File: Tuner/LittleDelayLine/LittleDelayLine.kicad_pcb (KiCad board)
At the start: 2 copper layers, 100 x 100 mm, 114 parts, among them J1 Conn_Coaxial, J10 Conn_Coaxial, J11 Conn_02x05_Odd_Even, J12 Conn_01x01, J13 Conn_01x01, J14 Conn_01x01, J15 Conn_01x01, J16 Conn_01x01, J17 Conn_Coaxial, J18 Conn_01x01, J19 Conn_01x01, J2 Conn_Coaxial, J20 Conn_01x01, J21 Conn_01x01, J22 Conn_Coaxial, J23 Conn_Coaxial, J24 Conn_Coaxial, J25 Conn_01x01, J26 Conn_01x01, J27 Conn_01x01, J3 Conn_Coaxial, J4 Conn_Coaxial, J5 Conn_Coaxial, J6 Conn_Coaxial, J7 Conn_Coaxial, J8 Conn_01x02, J9 Conn_01x02, P10 Conn_01x01, P11 Conn_01x01, P12 Conn_01x01, P2 Conn_01x01, P3 Conn_01x01, P4 Conn_01x01, P5 Conn_01x01, P6 Conn_01x01, P7 Conn_01x01, P8 Conn_01x01, P9 Conn_01x01, U1 MCP23008, U2 ULN2803A

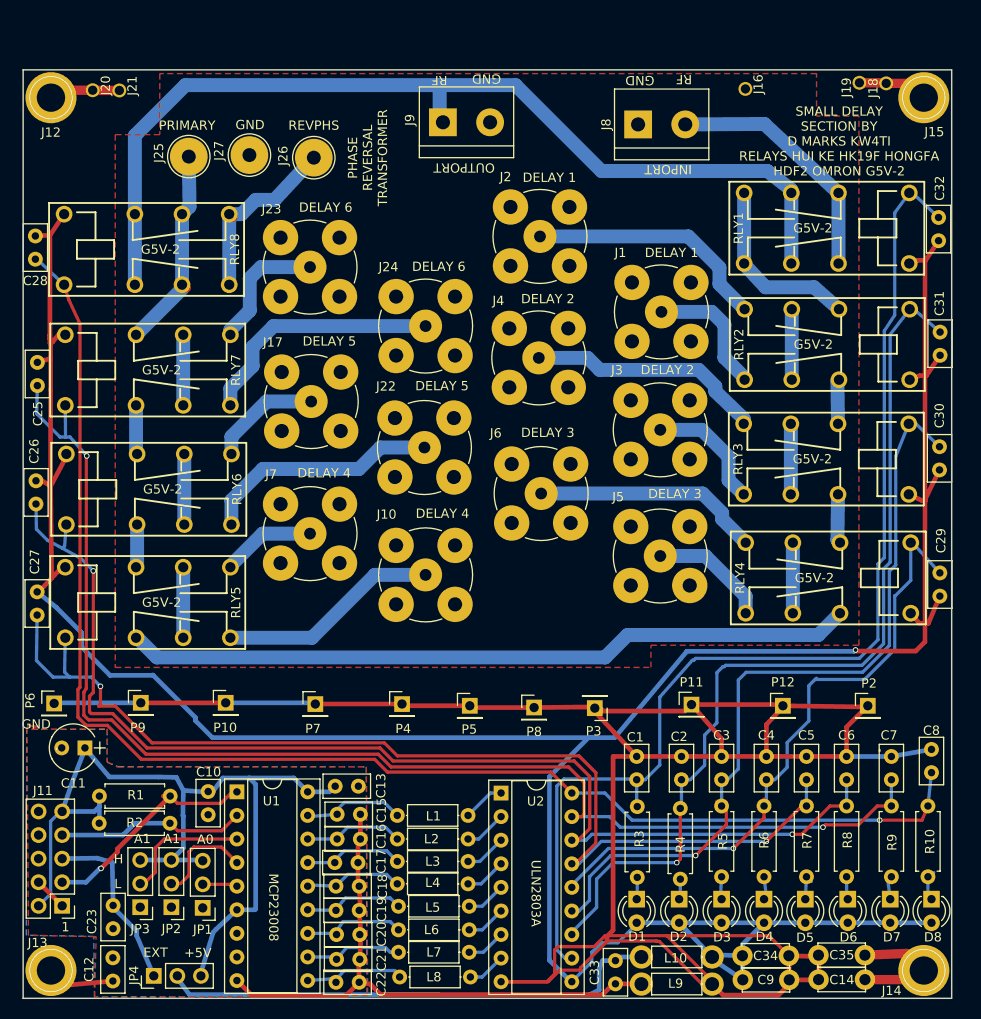
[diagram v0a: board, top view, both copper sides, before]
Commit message: Added more instrumentation to TandemMatch, fixed grounding issue
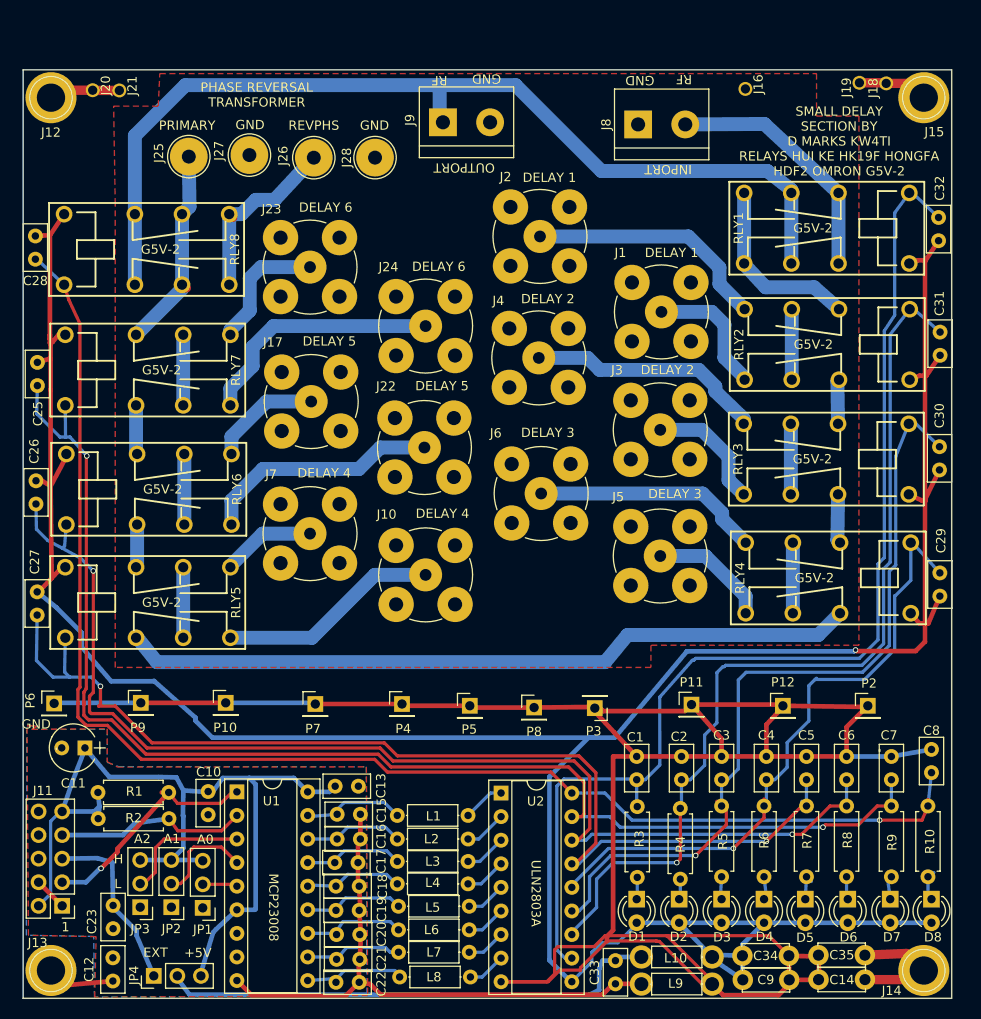
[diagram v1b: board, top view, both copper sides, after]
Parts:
- added J28: Conn_01x01, Connectors:1pin, F.Cu at (87.9, 59.5)
- R1, R2: value 1k -> 10k
- moved R2 0.50 mm to (58.1, 130.6)
- moved R1 0.42 mm to (58.1, 127.8)
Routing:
- net Net-(RLY4-Pad2): track 78.7 -> 79.4 mm
- net SCL: track 24.5 -> 25.0 mm
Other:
- board text added: "A2"
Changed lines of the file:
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@@
 (kicad_pcb (version 4) (host pcbnew 4.0.7)
   (general
-    (links 255)
+    (links 256)
     (no_connects 0)
-    (area 49.924999 49.924999 150.075001 150.075001)
+    (area 44.281218 46.80968 152.3901 153.921938)
     (thickness 1.6)
-    (drawings 40)
+    (drawings 41)
     (tracks 728)
     (zones 0)
-    (modules 114)
+    (modules 115)
     (nets 77)
   )
@@
   )
   (setup
-    (last_trace_width 0.5)
+    (last_trace_width 0.25)
     (user_trace_width 0.35)
     (user_trace_width 0.5)
@@
   )
   (module Resistors_THT:R_Axial_DIN0207_L6.3mm_D2.5mm_P7.62mm_Horizontal (layer F.Cu)
-    (at 58.2168 128.2192)
+    (at 58.05932 127.8255)
     (descr "Resistor, Axial_DIN0207 series, Axial, Horizontal, pin pitch=7.62mm, 0.25W = 1/4W, length*diameter=6.3*2.5mm^2, http://cdn-reichelt.de/documents/datenblatt/B400/1_4W%23YAG.pdf")
     (tags "Resistor Axial_DIN0207 series Axial Horizontal pin pitch 7.62mm 0.25W = 1/4W length 6.3mm diameter 2.5mm")
@@
       (effects (font (size 1 1) (thickness 0.15)))
     )
-    (fp_text value 1k (at 3.81 2.31) (layer F.Fab)
+    (fp_text value 10k (at 3.81 2.31) (layer F.Fab)
       (effects (font (size 1 1) (thickness 0.15)))
     )
@@
   )
   (module Resistors_THT:R_Axial_DIN0207_L6.3mm_D2.5mm_P7.62mm_Horizontal (layer F.Cu)
-    (at 58.1914 131.1402)
+    (at 58.08726 130.64744)
     (descr "Resistor, Axial_DIN0207 series, Axial, Horizontal, pin pitch=7.62mm, 0.25W = 1/4W, length*diameter=6.3*2.5mm^2, http://cdn-reichelt.de/documents/datenblatt/B400/1_4W%23YAG.pdf")
     (tags "Resistor Axial_DIN0207 series Axial Horizontal pin pitch 7.62mm 0.25W = 1/4W length 6.3mm diameter 2.5mm")
@@
       (effects (font (size 1 1) (thickness 0.15)))
     )
-    (fp_text value 1k (at 3.81 2.31) (layer F.Fab)
+    (fp_text value 10k (at 3.81 2.31) (layer F.Fab)
       (effects (font (size 1 1) (thickness 0.15)))
     )
@@
     )
   )
+  (module Connectors:1pin (layer F.Cu)
+    (at 87.89924 59.45632 90)
+    (descr "module 1 pin (ou trou mecanique de percage)")
+    (tags DEV)
+    (fp_text reference J28 (at 0 -3.048 90) (layer F.SilkS)
+      (effects (font (size 1 1) (thickness 0.15)))
+    )
+    (fp_text value Conn_01x01 (at 0 3 90) (layer F.Fab)
+      (effects (font (size 1 1) (thickness 0.15)))
+    )
+    (fp_circle (center 0 0) (end 2 0.8) (layer F.Fab) (width 0.1))
+    (fp_circle (center 0 0) (end 2.6 0) (layer F.CrtYd) (width 0.05))
+    (fp_circle (center 0 0) (end 0 -2.286) (layer F.SilkS) (width 0.12))
+    (pad 1 thru_hole circle (at 0 0 90) (size 4.064 4.064) (drill 1.5) (layers *.Cu *.Mask)
+      (net 1 RFGND))
+  )
+  (gr_text GND (at 87.84336 55.99176) (layer F.SilkS)
+    (effects (font (size 1 1) (thickness 0.15)))
+  )
   (gr_text OUTPORT (at 97.4979 60.5409 180) (layer F.SilkS)
     (effects (font (size 1 1) (thickness 0.15)))
   )
-  (gr_text "PHASE\nREVERSAL\nTRANSFORMER" (at 87.122 59.4741 90) (layer F.SilkS)
+  (gr_text "PHASE REVERSAL\nTRANSFORMER" (at 75.1586 52.69484) (layer F.SilkS)
     (effects (font (size 1 1) (thickness 0.15)))
   )
@@
     (effects (font (size 1 1) (thickness 0.15)))
   )
-  (gr_text A1 (at 62.8396 132.8166) (layer F.SilkS)
+  (gr_text A2 (at 62.8396 132.8166) (layer F.SilkS)
     (effects (font (size 1 1) (thickness 0.15)))
   )
@@
   (segment (start 54.2036 129.87528) (end 57.66562 129.87528) (width 0.5) (layer B.Cu) (net 19))
   (segment (start 57.66562 129.87528) (end 58.2168 129.3241) (width 0.5) (layer B.Cu) (net 19))
-  (segment (start 58.2168 128.2192) (end 58.2168 129.3241) (width 0.5) (layer B.Cu) (net 19))
-  (segment (start 58.2168 129.3241) (end 58.2168 131.1148) (width 0.5) (layer B.Cu) (net 19))
-  (segment (start 58.2168 131.1148) (end 58.1914 131.1402) (width 0.5) (layer B.Cu) (net 19))
+  (segment (start 58.05932 127.8255) (end 58.2168 129.3241) (width 0.5) (layer B.Cu) (net 19) (status 10))
+  (segment (start 58.2168 129.3241) (end 58.11266 130.62204) (width 0.5) (layer B.Cu) (net 19) (status 20))
+  (segment (start 58.11266 130.62204) (end 58.08726 130.64744) (width 0.5) (layer B.Cu) (net 19) (status 30))
   (segment (start 54.2036 129.87528) (end 54.02072 129.87528) (width 0.35) (layer B.Cu) (net 19) (status 30))
   (segment (start 54.02072 129.87528) (end 52.959 130.937) (width 0.35) (layer B.Cu) (net 19) (status 10))
@@
   (segment (start 54.8743 103.8987) (end 54.5414 103.5658) (width 0.5) (layer B.Cu) (net 32) (status 30))
   (segment (start 51.4985 94.3737) (end 51.3842 94.2594) (width 0.5) (layer B.Cu) (net 32) (status 30))
-  (segment (start 64.008 115.2144) (end 59.3598 115.2144) (width 0.5) (layer B.Cu) (net 32))
-  (segment (start 59.3598 115.2144) (end 56.3118 112.1664) (width 0.5) (layer B.Cu) (net 32))
+  (segment (start 64.135 115.8494) (end 59.4868 115.8494) (width 0.5) (layer B.Cu) (net 32))
+  (segment (start 59.4868 115.8494) (end 56.3118 112.1664) (width 0.5) (layer B.Cu) (net 32))
   (segment (start 53.5813 107.8992) (end 51.5112 106.2228) (width 0.5) (layer B.Cu) (net 32) (status 20))
-  (segment (start 63.9572 115.1636) (end 64.008 115.2144) (width 0.5) (layer B.Cu) (net 32))
-  (segment (start 64.008 115.2144) (end 68.58 119.7864) (width 0.5) (layer B.Cu) (net 32))
+  (segment (start 64.0842 115.7986) (end 64.135 115.8494) (width 0.5) (layer B.Cu) (net 32))
+  (segment (start 64.135 115.8494) (end 68.58 119.7864) (width 0.5) (layer B.Cu) (net 32))
   (segment (start 68.58 120.1166) (end 70.3834 121.92) (width 0.5) (layer B.Cu) (net 32))
   (segment (start 68.58 119.7864) (end 68.58 120.1166) (width 0.5) (layer B.Cu) (net 32))
@@
   (segment (start 57.9882 134.8994) (end 59.6011 135.3693) (width 0.5) (layer B.Cu) (net 51))
   (segment (start 54.2036 137.49528) (end 56.77662 137.49528) (width 0.5) (layer B.Cu) (net 52))
-  (segment (start 60.1472 133.9088) (end 65.8368 128.2192) (width 0.5) (layer F.Cu) (net 52))
+  (segment (start 60.1472 133.9088) (end 65.67932 127.8255) (width 0.5) (layer F.Cu) (net 52) (status 20))
   (segment (start 60.1472 134.2517) (end 60.1472 133.9088) (width 0.5) (layer F.Cu) (net 52))
   (segment (start 58.3946 136.0043) (end 60.1472 134.2517) (width 0.5) (layer F.Cu) (net 52))
@@
   (segment (start 72.5297 127.762) (end 71.2851 129.0066) (width 0.35) (layer F.Cu) (net 52))
   (segment (start 71.2851 129.0066) (end 66.6242 129.0066) (width 0.35) (layer F.Cu) (net 52))
-  (segment (start 66.6242 129.0066) (end 65.8368 128.2192) (width 0.35) (layer F.Cu) (net 52))
-  (segment (start 65.0875 128.2192) (end 65.8368 128.2192) (width 0.5) (layer F.Cu) (net 52))
-  (segment (start 65.8114 131.1402) (end 65.8368 131.1402) (width 0.35) (layer F.Cu) (net 53))
-  (segment (start 65.8368 131.1402) (end 66.6496 131.953) (width 0.35) (layer F.Cu) (net 53))
+  (segment (start 66.6242 129.0066) (end 65.67932 127.8255) (width 0.35) (layer F.Cu) (net 52) (status 20))
+  (segment (start 64.93002 127.8255) (end 65.67932 127.8255) (width 0.5) (layer F.Cu) (net 52) (status 30))
+  (segment (start 65.70726 130.64744) (end 65.73266 130.64744) (width 0.35) (layer F.Cu) (net 53) (status 30))
+  (segment (start 65.73266 130.64744) (end 66.6496 131.953) (width 0.35) (layer F.Cu) (net 53) (status 10))
   (segment (start 71.374 131.953) (end 73.025 130.302) (width 0.35) (layer F.Cu) (net 53))
   (segment (start 66.6496 131.953) (end 71.374 131.953) (width 0.35) (layer F.Cu) (net 53))
   (segment (start 54.2036 132.41528) (end 60.75172 132.41528) (width 0.5) (layer B.Cu) (net 53))
-  (segment (start 62.0268 131.1402) (end 65.8114 131.1402) (width 0.5) (layer B.Cu) (net 53))
+  (segment (start 62.0268 131.1402) (end 65.70726 130.64744) (width 0.5) (layer B.Cu) (net 53) (status 20))
   (segment (start 60.75172 132.41528) (end 62.0268 131.1402) (width 0.5) (layer B.Cu) (net 53))
   (segment (start 54.2036 132.41528) (end 54.89702 132.41528) (width 0.35) (layer B.Cu) (net 53) (status 30))
@@
   (segment (start 132.682 95.7226) (end 132.682 88.1226) (width 1.5) (layer B.Cu) (net 69))
   (segment (start 62.1614 111.1658) (end 62.2962 111.1658) (width 1.5) (layer B.Cu) (net 70))
-  (segment (start 62.2962 111.1658) (end 64.4144 113.284) (width 1.5) (layer B.Cu) (net 70))
-  (segment (start 64.4144 113.284) (end 112.6744 113.284) (width 1.5) (layer B.Cu) (net 70))
-  (segment (start 112.6744 113.284) (end 115.0874 110.871) (width 1.5) (layer B.Cu) (net 70))
+  (segment (start 62.2962 111.1658) (end 64.4144 113.792) (width 1.5) (layer B.Cu) (net 70))
+  (segment (start 64.4144 113.792) (end 112.6744 113.792) (width 1.5) (layer B.Cu) (net 70))
+  (segment (start 112.6744 113.792) (end 115.0874 110.871) (width 1.5) (layer B.Cu) (net 70))
   (segment (start 115.0874 110.871) (end 135.6311 110.871) (width 1.5) (layer B.Cu) (net 70))
   (segment (start 135.6311 110.871) (end 137.9779 108.5242) (width 1.5) (layer B.Cu) (net 70))
@@
     (polygon
       (pts
-        (xy 59.9186 64.3636) (xy 59.9186 114.3635) (xy 117.6147 114.3635) (xy 117.6147 111.9759) (xy 140.0175 111.9759)
-        (xy 140.0175 54.9783) (xy 135.4455 54.9783) (xy 135.4455 50.4063) (xy 64.7192 50.4063) (xy 64.7192 56.9849)
-        (xy 59.9186 56.9849) (xy 59.9186 64.4525)
+        (xy 135.4455 54.9783) (xy 140.0175 54.9783) (xy 140.0175 111.9759) (xy 117.6147 111.9759) (xy 117.6147 114.3635)
+        (xy 59.9186 114.3635) (xy 59.9186 64.4525) (xy 59.75096 53.9115) (xy 64.55156 53.9115) (xy 64.7192 50.4063)
+        (xy 135.4455 50.4063)
       )
     )

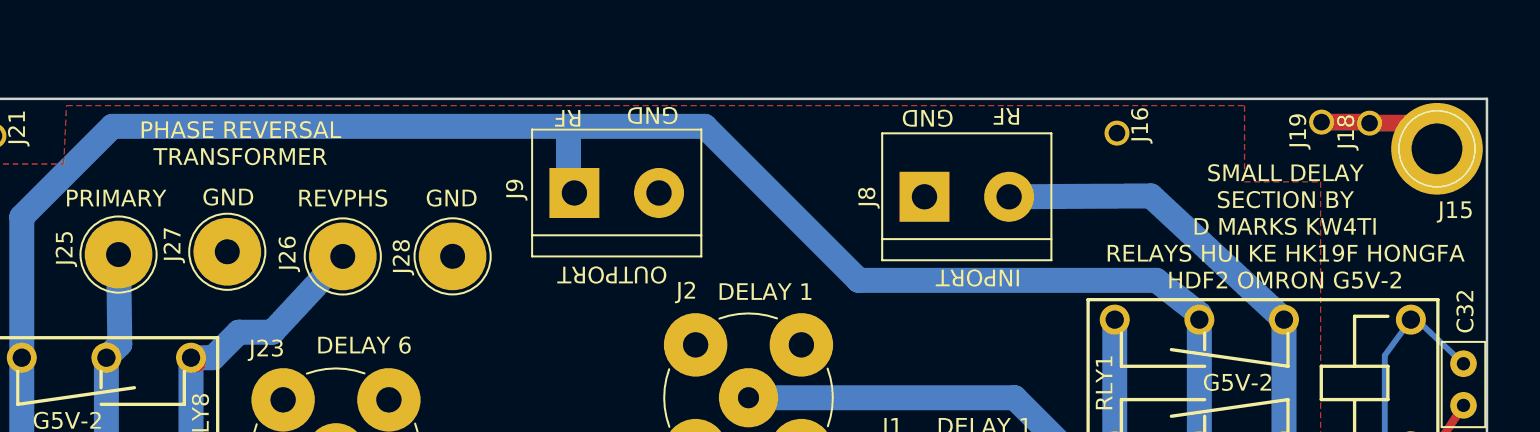
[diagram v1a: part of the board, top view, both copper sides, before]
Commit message: Added BNC and screw terminal combo pads
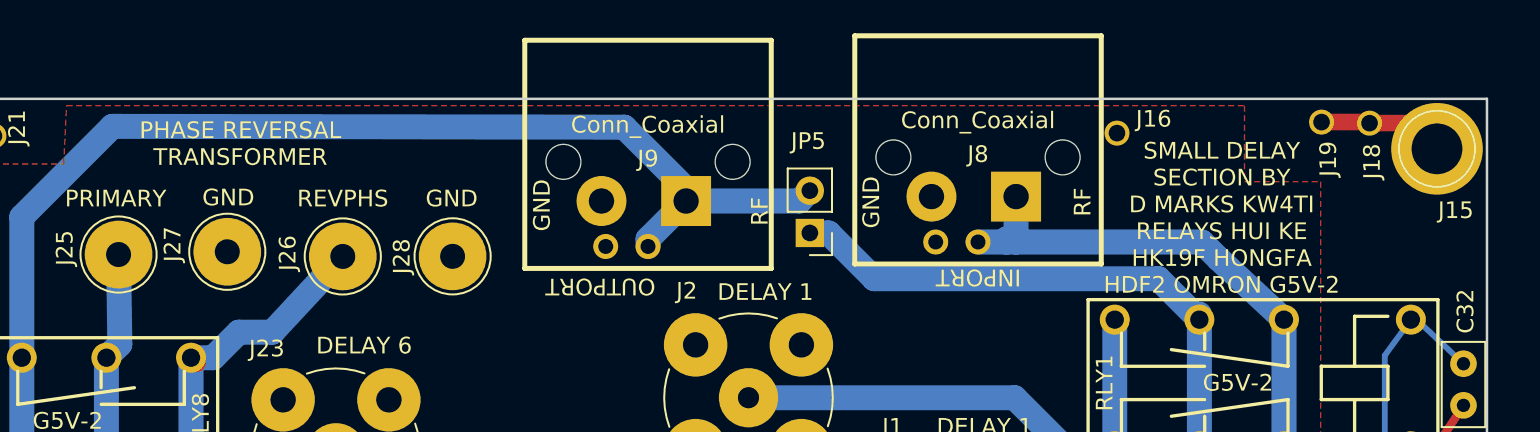
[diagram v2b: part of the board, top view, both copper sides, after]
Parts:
- added JP5: Jumper_NC_Small, Pin_Headers:Pin_Header_Straight_1x02_Pitch2.54mm, F.Cu at (109.3, 58.1)
- J8, J9: value Conn_01x02 -> Conn_Coaxial; footprint Connectors_Terminal_Blocks:TerminalBlock_bornier-2_P5.08mm -> tuner:bnc_90_1-1337543-0_pad_combo
- moved J8 10.2 mm to (119.4, 46.2), turned to 180 degrees
- moved J9 10.2 mm to (99.6, 46.5), turned to 180 degrees
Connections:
- J8 pad 1: RFGND -> Net-(J8-Pad1)
- J8 pad 2: Net-(J8-Pad2) -> RFGND
- RLY1 pad 2: Net-(J8-Pad2) -> Net-(J8-Pad1)
- RLY1 pad 3: RFOUT -> Net-(JP5-Pad1)
- RLY1 pad 6: Net-(J8-Pad2) -> Net-(J8-Pad1)
- RLY1 pad 7: RFOUT -> Net-(JP5-Pad1)
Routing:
- net RFOUT: track 106.4 -> 72.6 mm
- net Net-(JP5-Pad1): track 0.00 -> 33.5 mm
- net Net-(J8-Pad1): track 0.00 -> 31.4 mm
- net Net-(J8-Pad2): track 27.0 -> 0.00 mm
